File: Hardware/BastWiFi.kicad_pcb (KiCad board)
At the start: 2 copper layers, 60 x 22.9 mm, 35 parts, among them J1 Conn_Battery, J3 Conn_Left, J4 Conn_Right, P1 USB_C_Plug_USB2.0, Q1 DMG3415U-7, SW1 GPIO0, SW2 RESET, U1 MCP73831-3-OT, U2 AP2112K-3.3, U3 ESP32-S2-WROVER

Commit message: Add LED
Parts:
- added D3: LED, LED_SMD:LED_0603_1608Metric_Pad1.05x0.95mm_HandSolder, F.Cu at (131.7, 86.1)
- added R9: 1K, Resistor_SMD:R_0603_1608Metric_Pad1.05x0.95mm_HandSolder, F.Cu at (137.2, 91.5)
- moved SW1 0.31 mm to (140.5, 96.6)
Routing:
- net /GPIO13: track 4.13 -> 28.0 mm, vias 0 -> 1
- net Net-(D3-Pad1): track 0.00 -> 12.0 mm, vias 0 -> 2
- net VBUS: track 56.4 -> 50.2 mm
- net /EN: track 18.5 -> 19.4 mm
- net GND: track 117.7 -> 116.9 mm
- net +BATT: track 39.2 -> 38.4 mm
- net /D+: track 31.7 -> 31.1 mm
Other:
- board text added: "v1.1"

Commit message: Last Revision
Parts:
- removed SW1: GPIO0, Connectors EC:C455281
- added GPIO0: GPIO0, Connectors EC:C455281, F.Cu at (140.4, 97.5)
- moved RST 0.37 mm to (140.1, 101.4)
- renumbered SW2 to RST
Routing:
- net /GPIO0: track 46.6 -> 47.6 mm
- net /D+: track 31.1 -> 31.9 mm
- net /D-: track 33.6 -> 34.4 mm
- net Net-(P1-PadA5): track 10.3 -> 9.79 mm

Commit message: Last Revision
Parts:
- moved G*** 8.74 mm to (170.7, 93.3)
- renumbered GPIO0 to BOOT
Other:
- board text added: "10/10"
- board text added: "11/14"
- board text added: "12/13"
- board text added: "13/14"
- board text added: "5/07"
- board text added: "6/08"
- board text added: "9/09"
- board text added: "A0/01"
- board text added: "A1/02"
- board text added: "A2/03"
- board text added: "A3/04"
- board text added: "A4/05"
- board text added: "A5/06"
- board text added: "MISO/35"
- board text added: "MOSI/37"
- board text added: "SCK/36"
- board text added: "SCL/16"
- board text added: "SDA/15"
- board text removed: "10"
- board text removed: "11"
- board text removed: "12"
- board text removed: "13"
- board text removed: "5"
- board text removed: "6"
- board text removed: "9"
- board text removed: "A0"
- board text removed: "A1"
- board text removed: "A2"
- board text removed: "A3"
- board text removed: "A4"
- board text removed: "A5"
- board text removed: "MISO"
- board text removed: "MOSI"
- board text removed: "SCK"
- board text removed: "SCL"
- board text removed: "SDA"
- board text removed: "v1.0"

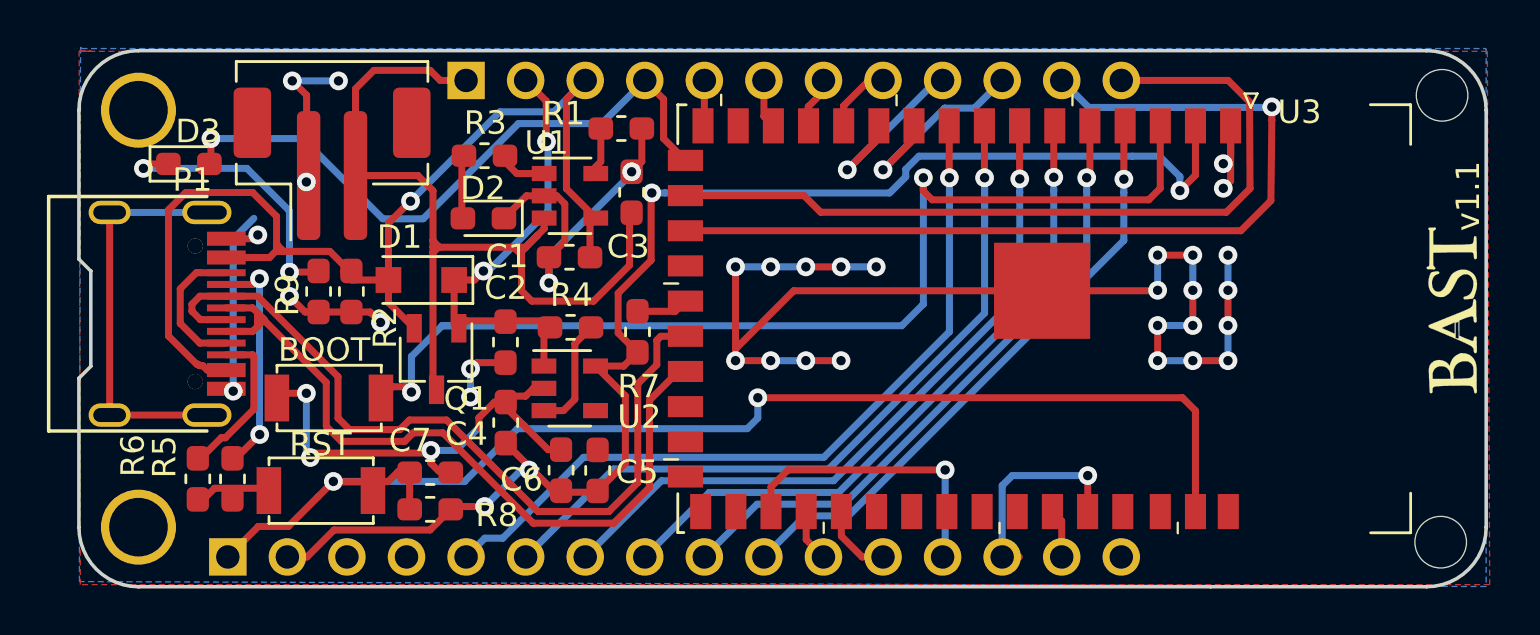
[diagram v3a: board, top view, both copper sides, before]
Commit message: Change pin
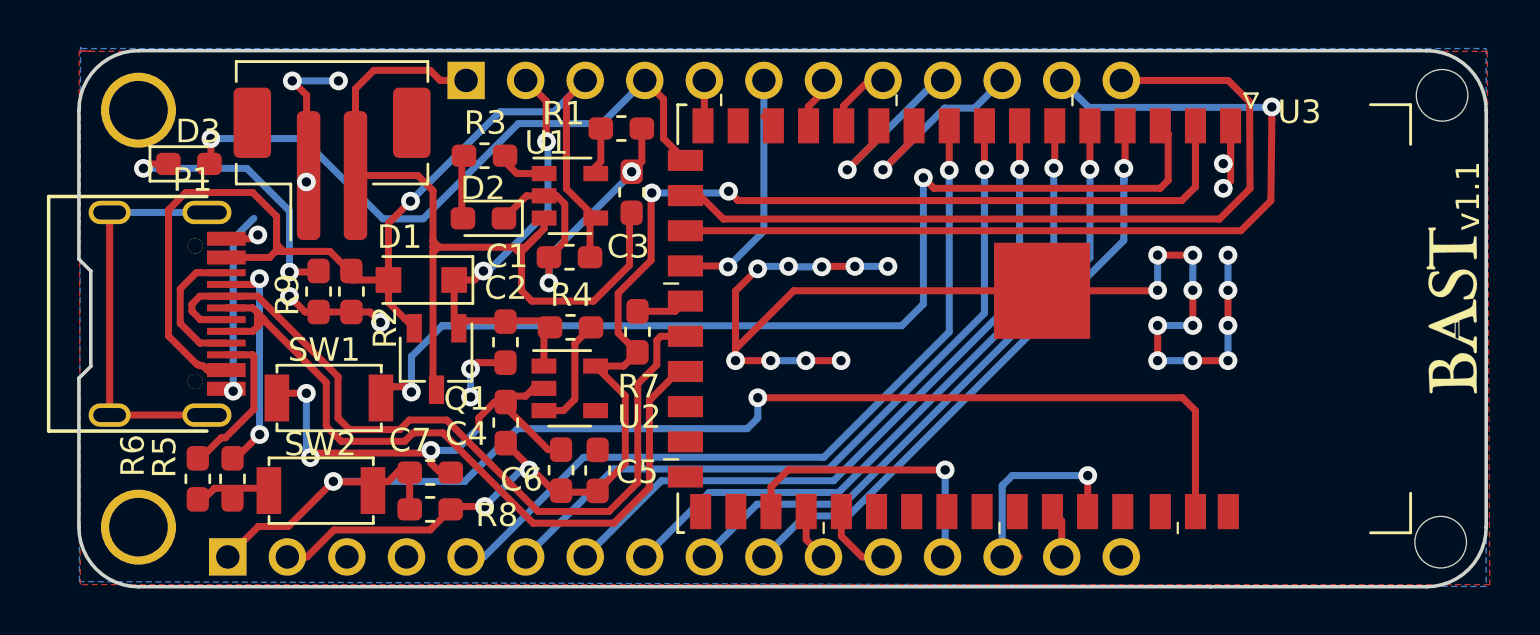
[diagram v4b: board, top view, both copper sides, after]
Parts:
- renumbered BOOT to SW1, RST to SW2
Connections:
- U3 pad 14: /GPIO11 -> Net-(U3-Pad14)
- U3 pad 20: Net-(U3-Pad20) -> /GPIO11
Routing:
- net /GPIO11: track 2.10 -> 10.4 mm, vias 0 -> 1
- net +3V3: track 60.1 -> 59.0 mm
- net Net-(U3-Pad14): track 0.00 -> 0.57 mm

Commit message: update v1.1
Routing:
- net /GPIO13: track 28.0 -> 32.6 mm
- net VBUS: track 50.2 -> 51.8 mm
- net /EN: track 19.4 -> 20.2 mm
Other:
- board text added: "Boot"
- board text added: "Reset"

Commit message: change pads
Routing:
- net Net-(U3-Pad14): track 0.57 -> 0.00 mm

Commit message: Last revision
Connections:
- net /Aref renamed Net-(J3-Pad3)
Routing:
- net /RX: track 9.14 -> 8.41 mm
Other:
- board text removed: "AREF"
